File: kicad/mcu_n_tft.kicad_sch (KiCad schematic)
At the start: 14 parts, among them Q1 SS8050-G, Q2 SS8050-G, SW2 SW_MEC_5G, U1 ESP32-S3-Rx

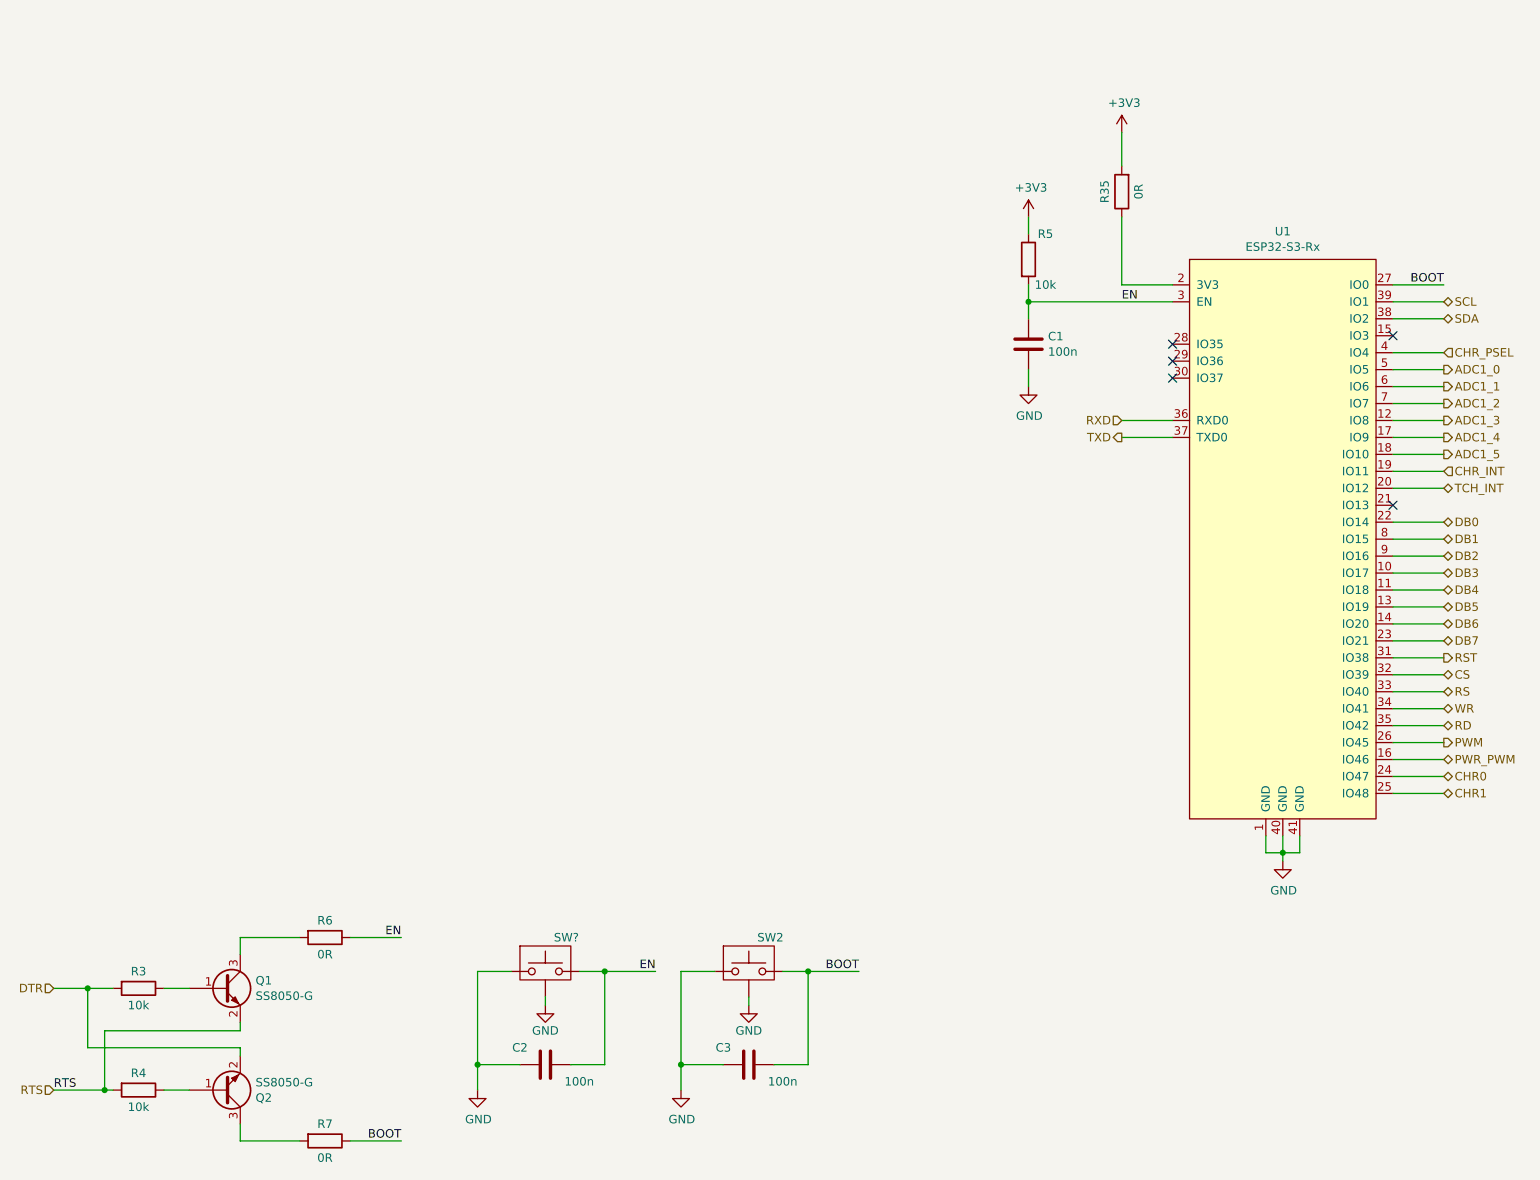
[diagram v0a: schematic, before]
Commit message: refactor KiCAD Project to v6
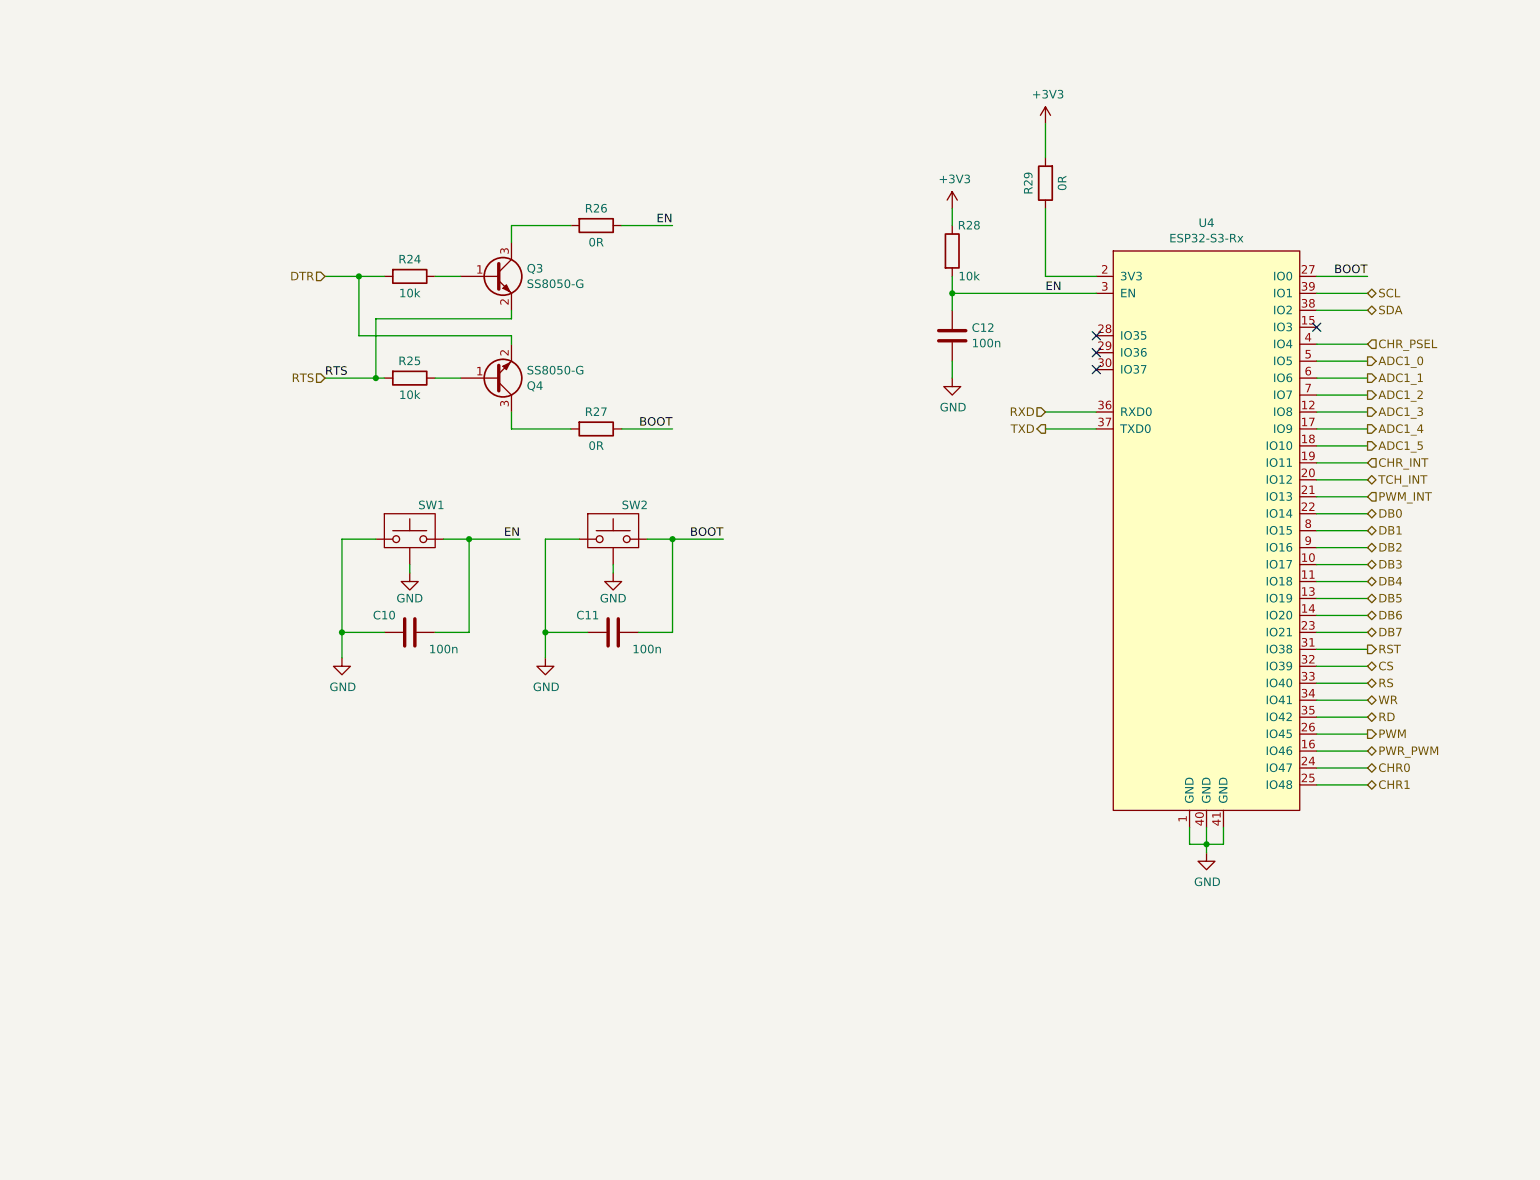
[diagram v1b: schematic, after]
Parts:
- removed C1, C2, C3: 100n, Capacitor_SMD:C_0603_1608Metric, symbol Device:C
- removed Q1, Q2: SS8050-G, Package_TO_SOT_SMD:SOT-23, symbol z_ic:SS8050-G
- removed R3, R4, R5: 10k, Resistor_SMD:R_0603_1608Metric, symbol Device:R
- removed R35, R6, R7: 0R, Resistor_SMD:R_0603_1608Metric, symbol Device:R
- removed SW?: SW_MEC_5G, z_connector:PTS820J25MSMTRLFS, symbol z_connectors:SW_MEC_5G
- removed U1: ESP32-S3-Rx, symbol z_ic:ESP32-S3-Rx
- added C10, C11, C12: 100n, Capacitor_SMD:C_0603_1608Metric, symbol Device:C
- added Q3, Q4: SS8050-G, Package_TO_SOT_SMD:SOT-23, symbol z_ic:SS8050-G
- added R24, R25, R28: 10k, Resistor_SMD:R_0603_1608Metric, symbol Device:R
- added R26, R27, R29: 0R, Resistor_SMD:R_0603_1608Metric, symbol Device:R
- added SW1: SW_MEC_5G, z_connector:PTS820J25MSMTRLFS, symbol z_connectors:SW_MEC_5G
- added U4: ESP32-S3-Rx, z_ic:ESP32-S3-WROOM-1, symbol z_ic:ESP32-S3-Rx
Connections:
- net +3V3: now also R28.1, R29.2
- net ADC1_0: now also U4.5 (IO5)
- net ADC1_1: now also U4.6 (IO6)
- net ADC1_2: now also U4.7 (IO7)
- net ADC1_3: now also U4.12 (IO8)
- net ADC1_4: now also U4.17 (IO9)
- net ADC1_5: now also U4.18 (IO10)
- net BOOT: now also C11.2, R27.1, U4.27 (IO0)
- net CHR0: now also U4.24 (IO47)
- net CHR1: now also U4.25 (IO48)
- net CHR_INT: now also U4.19 (IO11)
- net CHR_PSEL: now also U4.4 (IO4)
- net CS: now also U4.32 (IO39)
- net DB0: now also U4.22 (IO14)
- net DB1: now also U4.8 (IO15)
- net DB2: now also U4.9 (IO16)
- net DB3: now also U4.10 (IO17)
- net DB4: now also U4.11 (IO18)
- net DB5: now also U4.13 (IO19)
- net DB6: now also U4.14 (IO20)
- net DB7: now also U4.23 (IO21)
- net DTR: now also Q4.2 (E), R24.2
- net EN: now also C10.2, C12.1, R26.1, R28.2, SW1.2 (B), U4.3 (EN)
- net GND: now also C10.1, C11.1, C12.2, SW1.1 (A), SW1.3 (GND), U4.1 (GND), U4.40 (GND), U4.41 (GND)
- net PWM: now also U4.26 (IO45)
- net PWR_PWM: now also U4.16 (IO46)
- net RD: now also U4.35 (IO42)
- net RS: now also U4.33 (IO40)
- net RST: now also U4.31 (IO38)
- net RTS: now also Q3.2 (E), R25.2
- net RXD: now also U4.36 (RXD0)
- net SCL: now also U4.39 (IO1)
- net SDA: now also U4.38 (IO2)
- net TCH_INT: now also U4.20 (IO12)
- net TXD: now also U4.37 (TXD0)
- net WR: now also U4.34 (IO41)
- new net: Q3.1 (B), R24.1
- new net: Q3.3 (C), R26.2
- new net: R29.1, U4.2 (3V3)
- new net: Q4.1 (B), R25.1
- new net: Q4.3 (C), R27.2
- new net PWM_INT: U4.21 (IO13)
- no-connect marks 5 -> 4

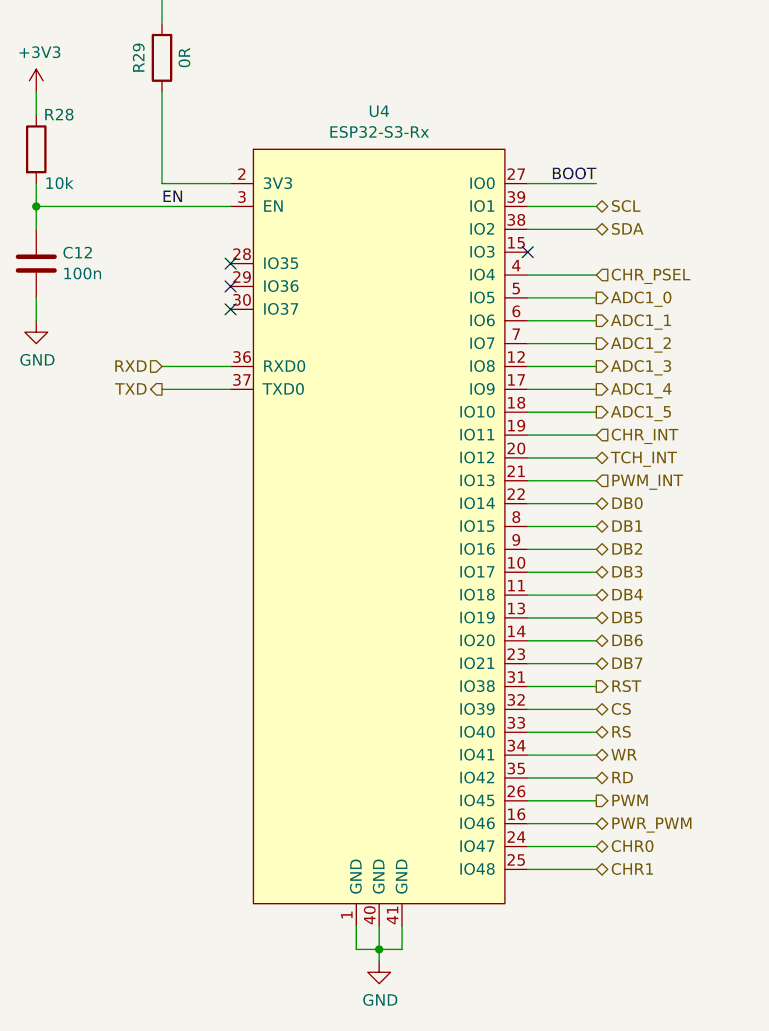
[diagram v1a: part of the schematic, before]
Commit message: add connection to lcd
import parts into pcbnew
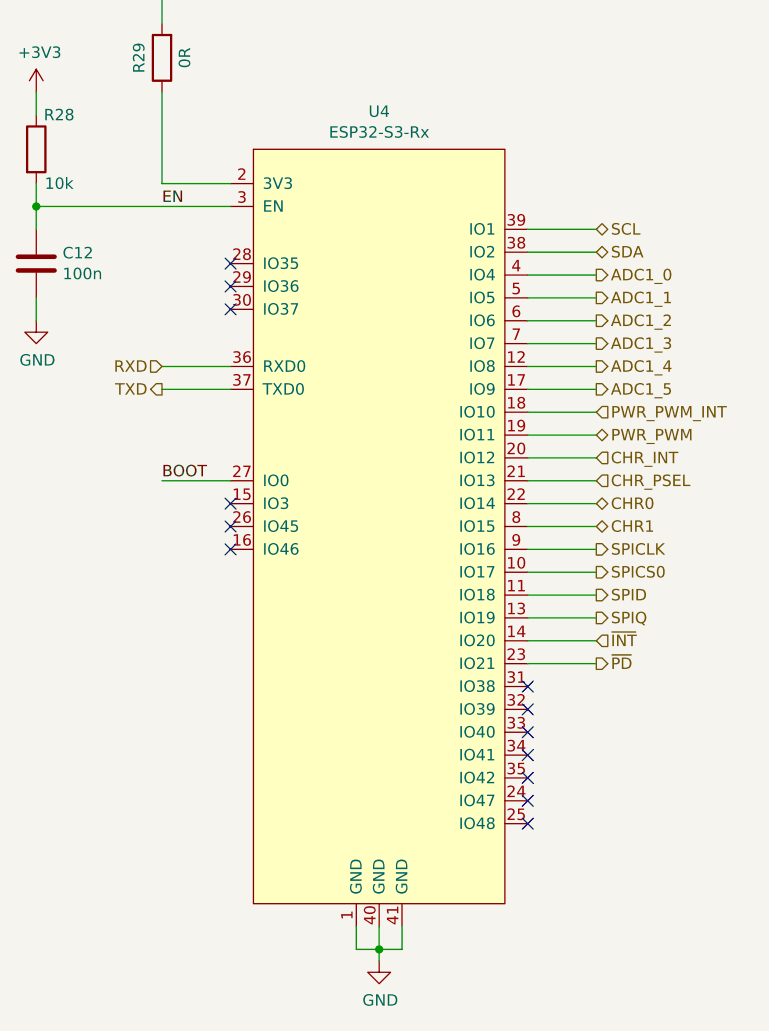
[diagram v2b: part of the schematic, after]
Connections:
- net DB0 is gone; now on net CHR0: U4.22 (IO14)
- net DB1 is gone; now on net CHR1: U4.8 (IO15)
- net PWM_INT is gone; now on net CHR_PSEL: U4.21 (IO13)
- net TCH_INT is gone; now on net CHR_INT: U4.20 (IO12)
- net ADC1_0: now also U4.4 (IO4); no longer U4.5 (IO5)
- net ADC1_1: now also U4.5 (IO5); no longer U4.6 (IO6)
- net ADC1_2: now also U4.6 (IO6); no longer U4.7 (IO7)
- net ADC1_3: now also U4.7 (IO7); no longer U4.12 (IO8)
- net ADC1_4: now also U4.12 (IO8); no longer U4.17 (IO9)
- net ADC1_5: now also U4.17 (IO9); no longer U4.18 (IO10)
- net CHR0: no longer U4.24 (IO47)
- net CHR1: no longer U4.25 (IO48)
- net CHR_INT: no longer U4.19 (IO11)
- net CHR_PSEL: no longer U4.4 (IO4)
- net PWR_PWM: now also U4.19 (IO11); no longer U4.16 (IO46)
- net CS: no longer names the net of U4.32 (IO39)
- net DB2 renamed SPICLK
- net DB3 renamed SPICS0
- net DB4 renamed SPID
- net DB5 renamed SPIQ
- net DB6 renamed ~{INT}
- net DB7 renamed ~{PD}
- net PWM: no longer names the net of U4.26 (IO45)
- net RD: no longer names the net of U4.35 (IO42)
- net RS: no longer names the net of U4.33 (IO40)
- net RST: no longer names the net of U4.31 (IO38)
- net WR: no longer names the net of U4.34 (IO41)
- new net PWR_PWM_INT: U4.18 (IO10)
- no-connect marks 4 -> 13

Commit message: route complete pcb
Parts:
- renumbered R24 to R28, R25 to R29, R26 to R30, R27 to R31, R28 to R32, R29 to R33
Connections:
- net ADC1_0: now also U4.17 (IO9); no longer U4.4 (IO4)
- net ADC1_1: now also U4.7 (IO7); no longer U4.5 (IO5)
- net ADC1_2: now also U4.5 (IO5); no longer U4.6 (IO6)
- net ADC1_3: now also U4.12 (IO8); no longer U4.7 (IO7)
- net ADC1_4: now also U4.6 (IO6); no longer U4.12 (IO8)
- net ADC1_5: now also U4.4 (IO4); no longer U4.17 (IO9)
- net CHR1: now also U4.23 (IO21); no longer U4.8 (IO15)
- net PWR_PWM: now also U4.18 (IO10); no longer U4.19 (IO11)
- net PWR_PWM_INT: now also U4.19 (IO11); no longer U4.18 (IO10)
- net ~{PD}: now also U4.8 (IO15); no longer U4.23 (IO21)
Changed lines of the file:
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@@
     (effects (font (size 1.27 1.27)) (justify right bottom))
   )
-  (hierarchical_label "ADC1_1" (shape output) (at 220.98 66.04 0)
+  (hierarchical_label "ADC1_1" (shape output) (at 220.98 71.12 0)
     (effects (font (size 1.27 1.27)) (justify left))
   )
@@
     (effects (font (size 1.27 1.27)) (justify left))
   )
-  (hierarchical_label "~{PD}" (shape output) (at 220.98 106.68 0)
+  (hierarchical_label "~{PD}" (shape output) (at 220.98 91.44 0)
     (effects (font (size 1.27 1.27)) (justify left))
   )
@@
     (effects (font (size 1.27 1.27)) (justify left))
   )
-  (hierarchical_label "PWR_PWM" (shape bidirectional) (at 220.98 81.28 0)
+  (hierarchical_label "PWR_PWM" (shape bidirectional) (at 220.98 78.74 0)
     (effects (font (size 1.27 1.27)) (justify left))
   )
@@
     (effects (font (size 1.27 1.27)) (justify right))
   )
-  (hierarchical_label "ADC1_4" (shape output) (at 220.98 73.66 0)
+  (hierarchical_label "ADC1_4" (shape output) (at 220.98 68.58 0)
     (effects (font (size 1.27 1.27)) (justify left))
   )
@@
     (effects (font (size 1.27 1.27)) (justify right))
   )
-  (hierarchical_label "ADC1_2" (shape output) (at 220.98 68.58 0)
+  (hierarchical_label "ADC1_2" (shape output) (at 220.98 66.04 0)
     (effects (font (size 1.27 1.27)) (justify left))
   )
@@
     (effects (font (size 1.27 1.27)) (justify left))
   )
-  (hierarchical_label "CHR1" (shape bidirectional) (at 220.98 91.44 0)
-    (effects (font (size 1.27 1.27)) (justify left))
-  )
-  (hierarchical_label "ADC1_0" (shape output) (at 220.98 63.5 0)
-    (effects (font (size 1.27 1.27)) (justify left))
-  )
-  (hierarchical_label "ADC1_5" (shape output) (at 220.98 76.2 0)
+  (hierarchical_label "CHR1" (shape bidirectional) (at 220.98 106.68 0)
+    (effects (font (size 1.27 1.27)) (justify left))
+  )
+  (hierarchical_label "ADC1_0" (shape output) (at 220.98 76.2 0)
+    (effects (font (size 1.27 1.27)) (justify left))
+  )
+  (hierarchical_label "ADC1_5" (shape output) (at 220.98 63.5 0)
     (effects (font (size 1.27 1.27)) (justify left))
   )
@@
     (effects (font (size 1.27 1.27)) (justify left))
   )
-  (hierarchical_label "PWR_PWM_INT" (shape input) (at 220.98 78.74 0)
+  (hierarchical_label "PWR_PWM_INT" (shape input) (at 220.98 81.28 0)
     (effects (font (size 1.27 1.27)) (justify left))
   )
@@
     (effects (font (size 1.27 1.27)) (justify right))
   )
-  (hierarchical_label "ADC1_3" (shape output) (at 220.98 71.12 0)
+  (hierarchical_label "ADC1_3" (shape output) (at 220.98 73.66 0)
     (effects (font (size 1.27 1.27)) (justify left))
   )
@@
   (symbol (lib_id "power:GND") (at 158.75 68.58 0) (unit 1)
     (in_bom yes) (on_board yes)
-    (property "Reference" "#PWR0153" (id 0) (at 158.75 74.93 0)
+    (property "Reference" "#PWR052" (id 0) (at 158.75 74.93 0)
       (effects (font (size 1.27 1.27)) hide)
     )
@@
   (symbol (lib_id "power:GND") (at 107.95 97.79 0) (unit 1)
     (in_bom yes) (on_board yes)
-    (property "Reference" "#PWR0149" (id 0) (at 107.95 104.14 0)
+    (property "Reference" "#PWR050" (id 0) (at 107.95 104.14 0)
       (effects (font (size 1.27 1.27)) hide)
     )
@@
   (symbol (lib_id "power:GND") (at 67.31 110.49 0) (unit 1)
     (in_bom yes) (on_board yes)
-    (property "Reference" "#PWR0148" (id 0) (at 67.31 116.84 0)
+    (property "Reference" "#PWR047" (id 0) (at 67.31 116.84 0)
       (effects (font (size 1.27 1.27)) hide)
     )
@@
   (symbol (lib_id "Device:R") (at 77.47 53.34 270) (unit 1)
     (in_bom yes) (on_board yes)
-    (property "Reference" "R24" (id 0) (at 77.47 50.8 90))
+    (property "Reference" "R28" (id 0) (at 77.47 50.8 90))
     (property "Value" "10k" (id 1) (at 77.47 55.88 90))
     (property "Footprint" "Resistor_SMD:R_0603_1608Metric" (id 2) (at 77.47 51.562 90)
@@
   (symbol (lib_id "Device:R") (at 172.72 39.37 180) (unit 1)
     (in_bom yes) (on_board yes)
-    (property "Reference" "R29" (id 0) (at 170.18 39.37 90))
+    (property "Reference" "R33" (id 0) (at 170.18 39.37 90))
     (property "Value" "0R" (id 1) (at 175.26 39.37 90))
     (property "Footprint" "Resistor_SMD:R_0603_1608Metric" (id 2) (at 174.498 39.37 90)
@@
   (symbol (lib_id "Device:R") (at 105.41 45.72 270) (unit 1)
     (in_bom yes) (on_board yes)
-    (property "Reference" "R26" (id 0) (at 105.41 43.18 90))
+    (property "Reference" "R30" (id 0) (at 105.41 43.18 90))
     (property "Value" "0R" (id 1) (at 105.41 48.26 90))
     (property "Footprint" "Resistor_SMD:R_0603_1608Metric" (id 2) (at 105.41 43.942 90)
@@
   (symbol (lib_id "Device:R") (at 158.75 49.53 0) (unit 1)
     (in_bom yes) (on_board yes)
-    (property "Reference" "R28" (id 0) (at 161.29 45.72 0))
+    (property "Reference" "R32" (id 0) (at 161.29 45.72 0))
     (property "Value" "10k" (id 1) (at 161.29 53.34 0))
     (property "Footprint" "Resistor_SMD:R_0603_1608Metric" (id 2) (at 156.972 49.53 90)
@@
   (symbol (lib_id "power:+3V3") (at 172.72 30.48 0) (unit 1)
     (in_bom yes) (on_board yes)
-    (property "Reference" "#PWR0151" (id 0) (at 172.72 34.29 0)
+    (property "Reference" "#PWR053" (id 0) (at 172.72 34.29 0)
       (effects (font (size 1.27 1.27)) hide)
     )
@@
   (symbol (lib_id "power:GND") (at 97.79 110.49 0) (unit 1)
     (in_bom yes) (on_board yes)
-    (property "Reference" "#PWR0147" (id 0) (at 97.79 116.84 0)
+    (property "Reference" "#PWR049" (id 0) (at 97.79 116.84 0)
       (effects (font (size 1.27 1.27)) hide)
     )
@@
   (symbol (lib_id "power:GND") (at 77.47 97.79 0) (unit 1)
     (in_bom yes) (on_board yes)
-    (property "Reference" "#PWR0150" (id 0) (at 77.47 104.14 0)
+    (property "Reference" "#PWR048" (id 0) (at 77.47 104.14 0)
       (effects (font (size 1.27 1.27)) hide)
     )
@@
   (symbol (lib_id "power:GND") (at 196.85 139.7 0) (unit 1)
     (in_bom yes) (on_board yes)
-    (property "Reference" "#PWR0146" (id 0) (at 196.85 146.05 0)
+    (property "Reference" "#PWR054" (id 0) (at 196.85 146.05 0)
       (effects (font (size 1.27 1.27)) hide)
     )
@@
   (symbol (lib_id "Device:R") (at 77.47 68.58 270) (unit 1)
     (in_bom yes) (on_board yes)
-    (property "Reference" "R25" (id 0) (at 77.47 66.04 90))
+    (property "Reference" "R29" (id 0) (at 77.47 66.04 90))
     (property "Value" "10k" (id 1) (at 77.47 71.12 90))
     (property "Footprint" "Resistor_SMD:R_0603_1608Metric" (id 2) (at 77.47 66.802 90)
@@
   (symbol (lib_id "power:+3V3") (at 158.75 43.18 0) (unit 1)
     (in_bom yes) (on_board yes)
-    (property "Reference" "#PWR0152" (id 0) (at 158.75 46.99 0)
+    (property "Reference" "#PWR051" (id 0) (at 158.75 46.99 0)
       (effects (font (size 1.27 1.27)) hide)
     )
@@
   (symbol (lib_id "Device:R") (at 105.41 76.2 270) (unit 1)
     (in_bom yes) (on_board yes)
-    (property "Reference" "R27" (id 0) (at 105.41 73.66 90))
+    (property "Reference" "R31" (id 0) (at 105.41 73.66 90))
     (property "Value" "0R" (id 1) (at 105.41 78.74 90))
     (property "Footprint" "Resistor_SMD:R_0603_1608Metric" (id 2) (at 105.41 74.422 90)
